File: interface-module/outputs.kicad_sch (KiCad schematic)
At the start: 28 parts, among them Q1 PMOS, Q10 NMOS, Q11 PMOS, Q12 NMOS, Q13 PMOS, Q14 NMOS, Q15 PMOS, Q16 NMOS, Q2 NMOS, Q3 PMOS, Q4 NMOS, Q5 PMOS, Q6 NMOS, Q7 PMOS, Q8 NMOS, Q9 PMOS, U2 140357145200, U3 140357145200, U4 140357145200, U5 140357145200, U6 140357145200, U7 140357145200, U8 140357145200, U9 140357145200

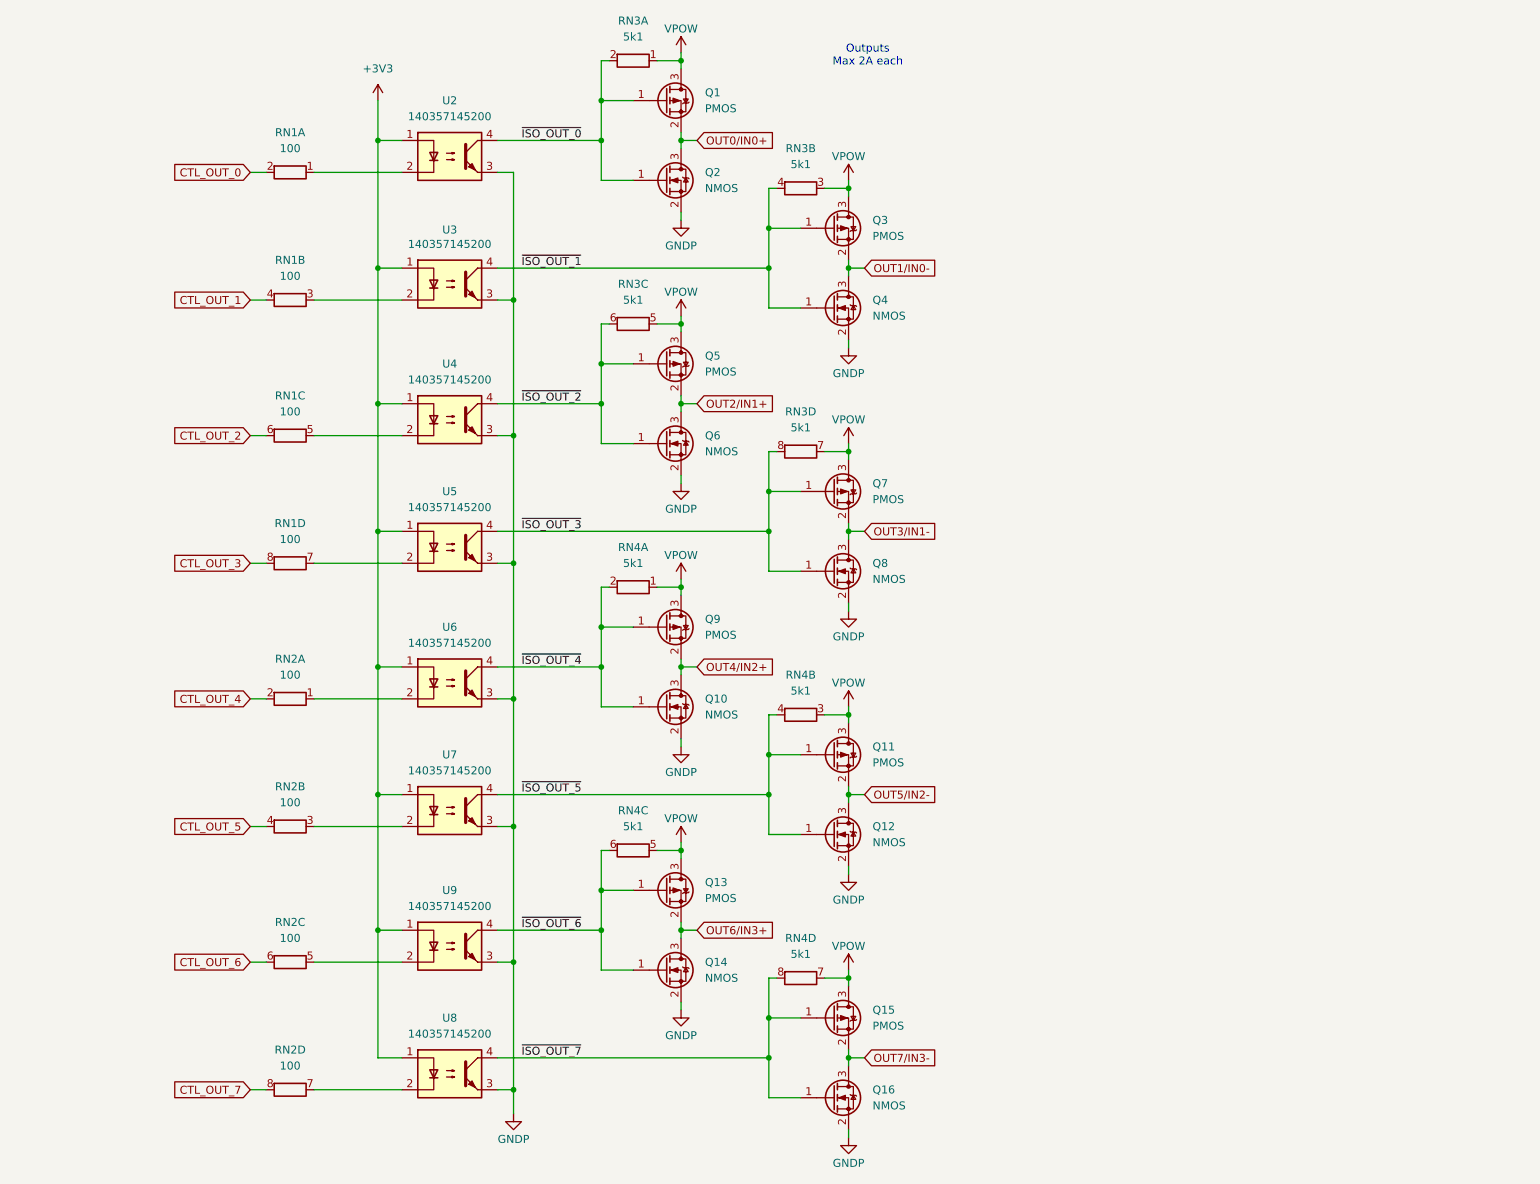
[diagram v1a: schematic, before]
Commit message: routed most of board
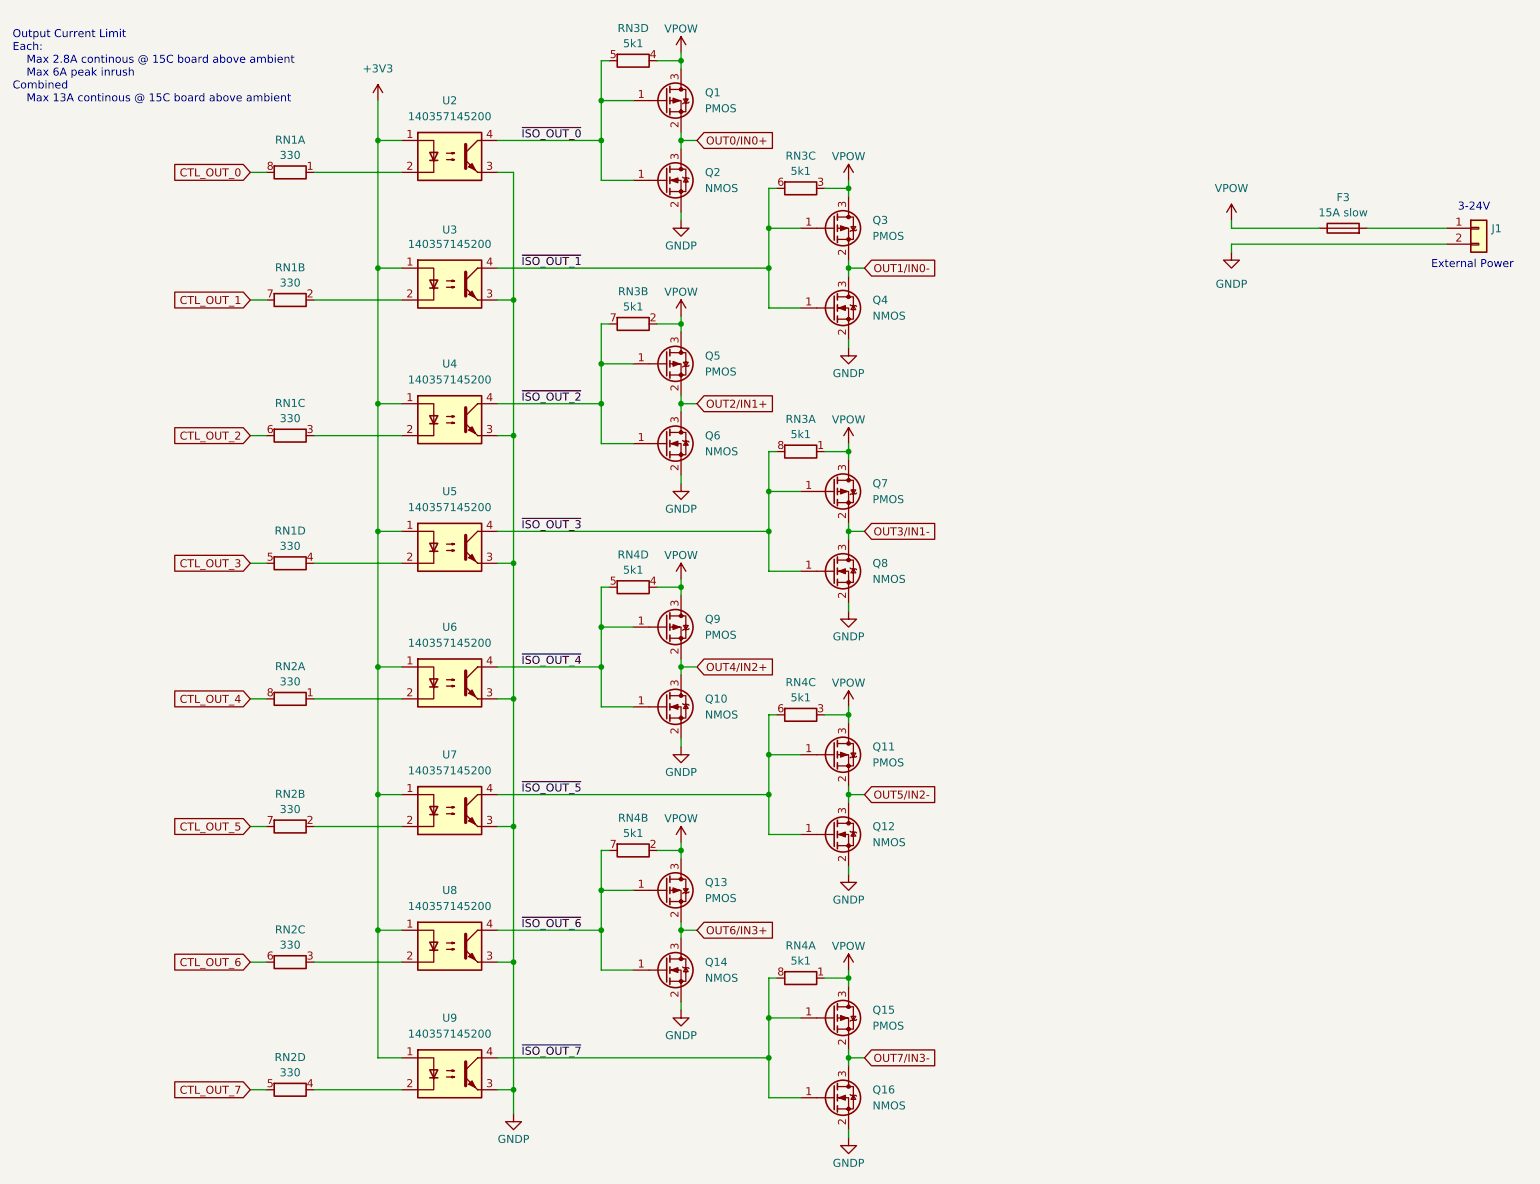
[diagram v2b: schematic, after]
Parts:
- added F3: 15A slow, Fuse:Fuseholder_Cylinder-5x20mm_Schurter_0031_8201_Horizontal_Open, symbol Device:Fuse
- added J1: Conn_01x02, TerminalBlock:TerminalBlock_bornier-2_P5.08mm, symbol Connector_Generic:Conn_01x02
- Q1, Q11, Q13, Q15, Q3, Q5, Q7, Q9: DPN 4786-SSF6911SCT-ND -> SSM3J378RLFCT-ND; MPN SSF6911S -> SSM3J378R,LF
- Q10, Q12, Q14, Q16, Q2, Q4, Q6, Q8: DPN 4530-AS2324CT-ND -> 31-DMN2053UQ-13CT-ND; MPN AS2324 -> DMN2053UQ-13
- RN1, RN2: value 100 -> 330; symbol Device:R_Pack04_SIP_Split -> Device:R_Pack04_Split; DPN CAY16-101J4LF -> CAY16-331J4LFCT-ND; MPN CAY16-101J4LFCT-ND -> CAY16-331J4LF
- RN3, RN4: symbol Device:R_Pack04_SIP_Split -> Device:R_Pack04_Split
- renumbered U9 to U8, U8 to U9
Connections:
- net CTL_OUT_0: now also RN1.8 (R1.2); no longer RN1.2 (R1.2)
- net CTL_OUT_1: now also RN1.7 (R2.2); no longer RN1.4 (R2.2)
- net CTL_OUT_3: now also RN1.5 (R4.2); no longer RN1.8 (R4.2)
- net CTL_OUT_4: now also RN2.8 (R1.2); no longer RN2.2 (R1.2)
- net CTL_OUT_5: now also RN2.7 (R2.2); no longer RN2.4 (R2.2)
- net CTL_OUT_7: now also RN2.5 (R4.2); no longer RN2.8 (R4.2)
- net GNDP: now also J1.2 (Pin_2)
- net VPOW: now also RN3.2 (R2.1), RN3.3 (R3.1), RN3.4 (R4.1), RN4.2 (R2.1), RN4.3 (R3.1), RN4.4 (R4.1), F3.1; no longer RN3.3 (R2.1), RN3.5 (R3.1), RN3.7 (R4.1), RN4.3 (R2.1), RN4.5 (R3.1), RN4.7 (R4.1)
- net ~{ISO_OUT_0}: now also RN3.5 (R4.2); no longer RN3.2 (R1.2)
- net ~{ISO_OUT_1}: now also RN3.6 (R3.2); no longer RN3.4 (R2.2)
- net ~{ISO_OUT_2}: now also RN3.7 (R2.2); no longer RN3.6 (R3.2)
- net ~{ISO_OUT_3}: now also RN3.8 (R1.2); no longer RN3.8 (R4.2)
- net ~{ISO_OUT_4}: now also RN4.5 (R4.2); no longer RN4.2 (R1.2)
- net ~{ISO_OUT_5}: now also RN4.6 (R3.2); no longer RN4.4 (R2.2)
- net ~{ISO_OUT_6}: now also RN4.7 (R2.2); no longer RN4.6 (R3.2)
- net ~{ISO_OUT_7}: now also RN4.8 (R1.2); no longer RN4.8 (R4.2)
- net at U7.2: now also RN2.2 (R2.1); no longer RN2.3 (R2.1)
- net at U8.2: now also RN2.3 (R3.1); no longer RN2.5 (R3.1)
- net at U3.2: now also RN1.2 (R2.1); no longer RN1.3 (R2.1)
- net at U9.2: now also RN2.4 (R4.1); no longer RN2.7 (R4.1)
- net at U4.2: now also RN1.3 (R3.1); no longer RN1.5 (R3.1)
- net at U5.2: now also RN1.4 (R4.1); no longer RN1.7 (R4.1)
- new net: F3.2, J1.1 (Pin_1)
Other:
- note added: "3-24V"
- note added: "External Power"
- note added: "Output Current Limit Each: Max 2.8A continous @ 15C board above ambient Max 6A peak inrush Combined Max 13A continous @ 15C board above ambient"
- note removed: "Outputs Max 2A each"
- moved on the sheet: RN3A, RN3B, RN3C, RN3D, RN4A, RN4B, RN4C, RN4D
